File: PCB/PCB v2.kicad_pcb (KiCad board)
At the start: 4 copper layers, 56 x 45 mm, 99 parts, among them J2 USB_C_Receptacle_PowerOnly_6P, J3 6871XX182122_687110182122, J5 Conn_01x03_Pin, J7 Conn_01x07_Pin, U1 TPD2E2U06DCK, U11 OPA4350EA_250, U12 OPA4350EA_250, U13 OPA4350EA_250, U4 LM27762, U5 AD7606, U6 OPA4350EA_250

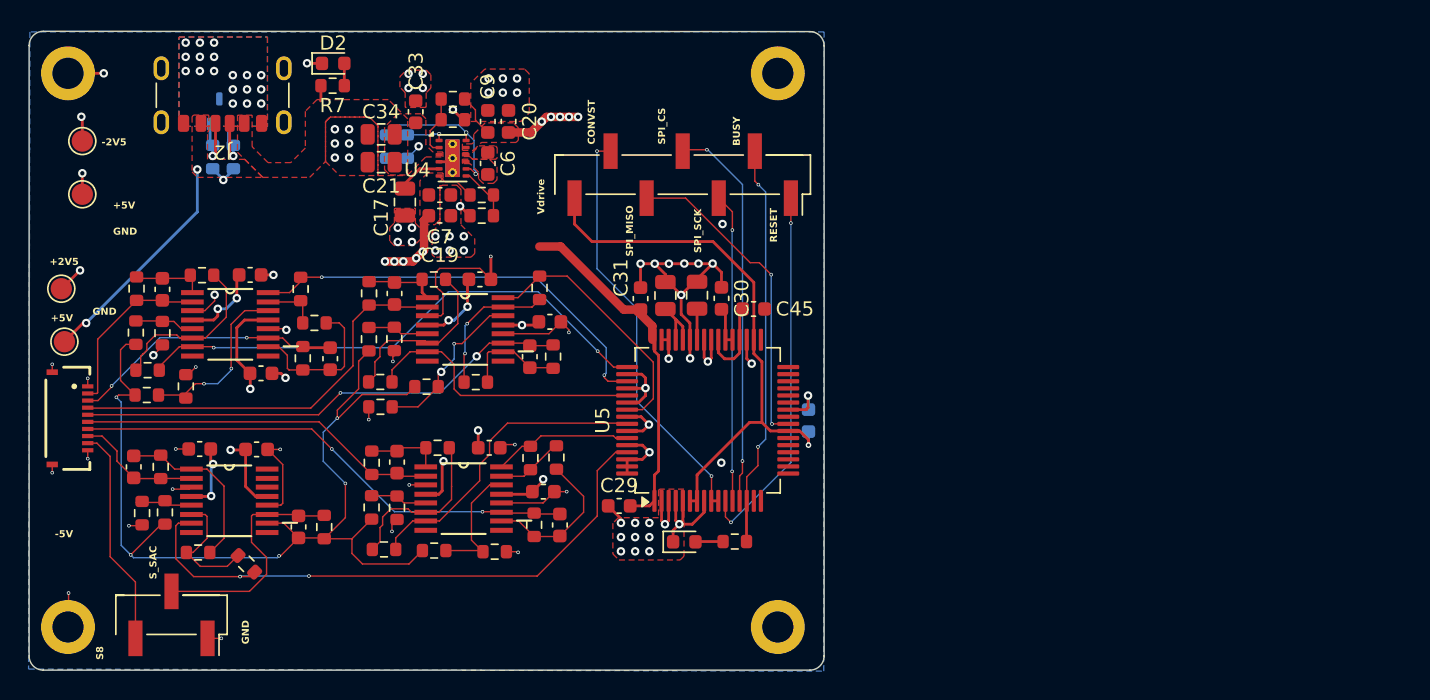
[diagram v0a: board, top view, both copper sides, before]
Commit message: Lay out the analog front-end: op-amp groups, sensor inputs, GND guard
Board work since d215e9c. The schematic changes were brought in with
Update PCB from Schematic; op-amp placement and some routing were done
by hand in pcbnew; the rest was scripted through the KiCad IPC API and
checked with offline DRC.

Op-amp groups (TIA and difference amps):
- U6: its Rf/Cf pairs sit right at each section's -IN/OUT pads, with the
  +2V5/-2V5 decoupling caps (C22/C11) on the bottom under the chip.
- U13: U6's placement, fan-out tracks and vias copied exactly
  (40 segments, 4 vias). Section mapping is A->A (S1->S7), B->B
  (S2->S_sac), C->C (S3->S5), D->D (S4->S6); C27/C28 are on the bottom.
- U11: the left half (CH1/CH2) was placed and routed by hand. The right
  half (CH3/CH4) is its mirror about the IC centre line, with pins
  1<->16, 2<->15, 3<->14, 5<->12, 6<->11 and 7<->10 (8 passives, C24,
  23 segments, 6 vias).
- U12: U11 copied at an offset of (-21.35, +3.00). CH1-3 became CH5-7
  (14 passives on the bottom, 42 segments, 13 vias). CH4's copper was
  not copied, because U12 section D is the spare. The spare is tied as a
  follower: pin 15 to pin 16 (SPARE_D), and pin 14 to a new GND via.
- U6 and U13 were then moved next to J3, U6 above and U13 below.

Sensor inputs J3 -> TIA nodes (S1-S7):
- All on F.Cu at 0.1 mm, with no vias and no crossings. Each trace
  enters its node at the Rf/Cf pad, never at the op-amp pin. Corners
  were rounded by hand.
- S1/S2 run up the left of U6 and over the top to C10/C12. S3-S6 use
  the corridor between U6 and U13, into C14/C13/C16/C15. S7 runs down
  the left of U13 and under it to C18.
- The routes were checked in an offline DRC before being applied: no
  new clearance, edge or hole violations.

GND guard around the inputs:
- New F.Cu zone GND_AFE_GUARD (priority 1, clearance 0.2, solid pad
  connection, islands removed). It covers x 125.9-136.6 and
  y 86.6-118.9, with a notch that takes in J3's GND pins.
- 31 GND stitching vias (0.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
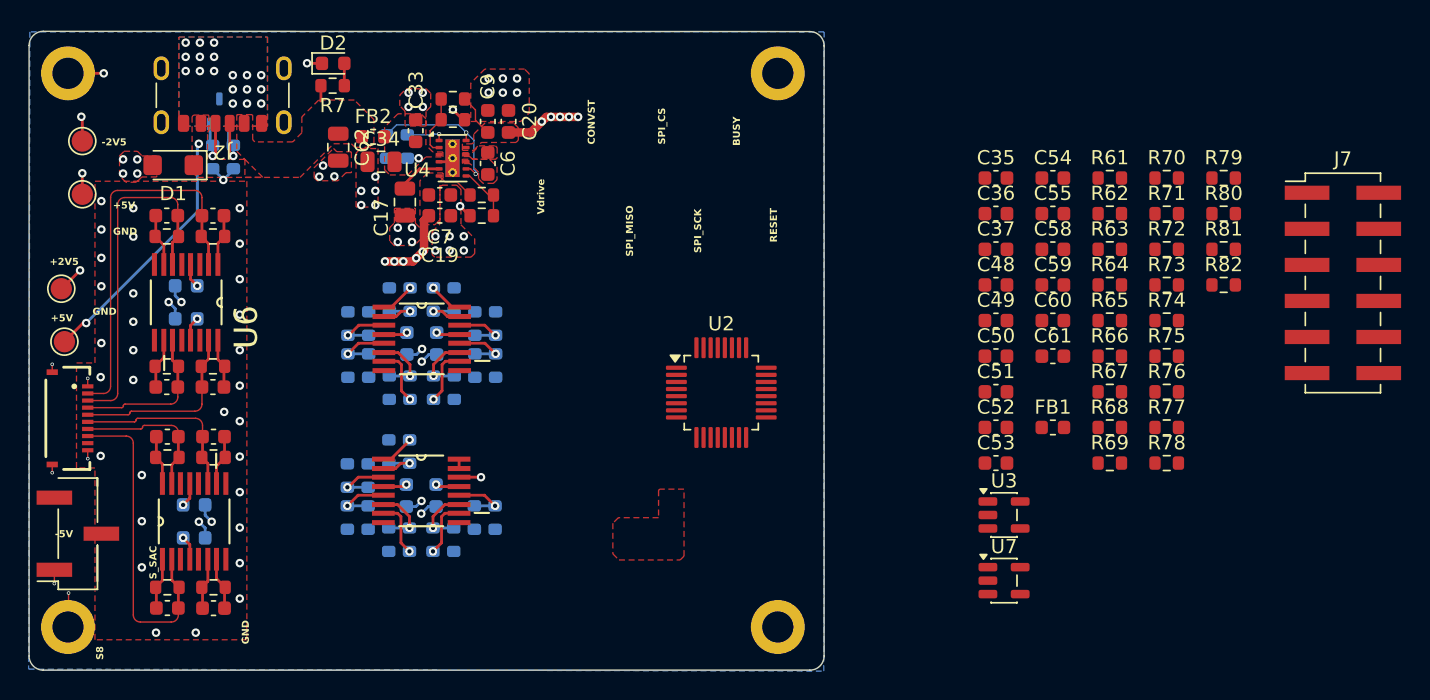
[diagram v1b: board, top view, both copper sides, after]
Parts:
- removed C21, C46, C47: 10u, Capacitor_SMD:C_0805_2012Metric
- removed C29, C30, C31, C32: 100n, Capacitor_SMD:C_0603_1608Metric
- removed C45: 1u, Capacitor_SMD:C_0603_1608Metric
- removed D3: LED, LED_SMD:LED_0603_1608Metric
- removed R8: 4.7k, Resistor_SMD:R_0603_1608Metric
- removed U5: AD7606, Package_QFP:LQFP-64_10x10mm_P0.5mm
- added C35: 220n, Capacitor_SMD:C_0603_1608Metric, F.Cu at (189.4, 86.4)
- added C36: 1u, Capacitor_SMD:C_0603_1608Metric, F.Cu at (189.4, 88.9)
- added C37: 1u, Capacitor_SMD:C_0603_1608Metric, F.Cu at (189.4, 91.4)
- added C48: 10n C0G, Capacitor_SMD:C_0603_1608Metric, F.Cu at (189.4, 93.9)
- added C49: 10n C0G, Capacitor_SMD:C_0603_1608Metric, F.Cu at (189.4, 96.4)
- added C50: 10n C0G, Capacitor_SMD:C_0603_1608Metric, F.Cu at (189.4, 98.9)
- added C51: 10n C0G, Capacitor_SMD:C_0603_1608Metric, F.Cu at (189.4, 101.4)
- added C52: 10n C0G, Capacitor_SMD:C_0603_1608Metric, F.Cu at (189.4, 103.9)
- added C53: 10n C0G, Capacitor_SMD:C_0603_1608Metric, F.Cu at (189.4, 106.5)
- added C54: 10n C0G, Capacitor_SMD:C_0603_1608Metric, F.Cu at (193.4, 86.4)
- added C55: 10n C0G, Capacitor_SMD:C_0603_1608Metric, F.Cu at (193.4, 88.9)
- added C58: 100n, Capacitor_SMD:C_0603_1608Metric, F.Cu at (193.4, 91.4)
- added C59: 100n, Capacitor_SMD:C_0603_1608Metric, F.Cu at (193.4, 93.9)
- added C60: 1u, Capacitor_SMD:C_0603_1608Metric, F.Cu at (193.4, 96.4)
- added C61: 1u, Capacitor_SMD:C_0603_1608Metric, F.Cu at (193.4, 98.9)
- added C62: 22u 16V, Capacitor_SMD:C_0805_2012Metric, F.Cu at (143.0, 84.2)
- added D1: SMF5.0A, Diode_SMD:D_SMF, F.Cu at (131.4, 85.5)
- added FB1: BLM18PG221SN1, Inductor_SMD:L_0603_1608Metric, F.Cu at (193.4, 103.9)
- added FB2: BLM18KG102SN1, Inductor_SMD:L_0603_1608Metric, F.Cu at (145.5, 83.5)
- added R61: 1.1k, Resistor_SMD:R_0603_1608Metric, F.Cu at (197.4, 86.4)
- added R62: 1k, Resistor_SMD:R_0603_1608Metric, F.Cu at (197.4, 88.9)
- added R63: 1.1k, Resistor_SMD:R_0603_1608Metric, F.Cu at (197.4, 91.4)
- added R64: 1k, Resistor_SMD:R_0603_1608Metric, F.Cu at (197.4, 93.9)
- added R65: 1.1k, Resistor_SMD:R_0603_1608Metric, F.Cu at (197.4, 96.4)
- added R66: 1k, Resistor_SMD:R_0603_1608Metric, F.Cu at (197.4, 98.9)
- added R67: 1.1k, Resistor_SMD:R_0603_1608Metric, F.Cu at (197.4, 101.4)
- added R68: 1k, Resistor_SMD:R_0603_1608Metric, F.Cu at (197.4, 103.9)
- added R69: 1.1k, Resistor_SMD:R_0603_1608Metric, F.Cu at (197.4, 106.5)
- added R70: 1k, Resistor_SMD:R_0603_1608Metric, F.Cu at (201.4, 86.4)
- added R71: 1.1k, Resistor_SMD:R_0603_1608Metric, F.Cu at (201.4, 88.9)
- added R72: 1k, Resistor_SMD:R_0603_1608Metric, F.Cu at (201.4, 91.4)
- added R73: 1.1k, Resistor_SMD:R_0603_1608Metric, F.Cu at (201.4, 93.9)
- added R74: 1k, Resistor_SMD:R_0603_1608Metric, F.Cu at (201.4, 96.4)
- added R75: 1.1k, Resistor_SMD:R_0603_1608Metric, F.Cu at (201.4, 98.9)
- added R76: 1k, Resistor_SMD:R_0603_1608Metric, F.Cu at (201.4, 101.4)
- added R77: 10k, Resistor_SMD:R_0603_1608Metric, F.Cu at (201.4, 103.9)
- added R78: 10k, Resistor_SMD:R_0603_1608Metric, F.Cu at (201.4, 106.5)
- added R79: 100k, Resistor_SMD:R_0603_1608Metric, F.Cu at (205.4, 86.4)
- added R80: 33R, Resistor_SMD:R_0603_1608Metric, F.Cu at (205.4, 88.9)
- added R81: 33R, Resistor_SMD:R_0603_1608Metric, F.Cu at (205.4, 91.4)
- added R82: 33R, Resistor_SMD:R_0603_1608Metric, F.Cu at (205.4, 93.9)
- added U2: ADS131M08xPBS, Package_QFP:TQFP-32_5x5mm_P0.5mm, F.Cu at (170.0, 101.5)
- added U3: 74LVC1G17, Package_TO_SOT_SMD:SOT-23-5, F.Cu at (189.9, 110.1)
- added U7: LP5907MFX-3.3, Package_TO_SOT_SMD:SOT-23-5, F.Cu at (189.9, 114.7)
- C11, C22, C23, C24, C25, C26, C27, C28, R24, R26, R29, R31, R34, R36, R38, R39, R44, R46, R48, R49, R56, R59: moved to B.Cu
- J7: value Conn_01x07_Pin -> Conn_02x06_Odd_Even; footprint Connector_PinHeader_2.54mm:PinHeader_1x07_P2.54mm_Vertical_SMD_Pin1Right -> Connector_PinHeader_2.54mm:PinHeader_2x06_P2.54mm_Vertical_SMD
- R23, R25, R28, R30, R33, R35, R40, R41, R43, R45, R50, R51, R55, R60: value 5k -> 4.99k; moved to B.Cu
- moved J7 47.1 mm to (213.8, 93.8), turned to 0 degrees
- moved C15 28.3 mm to (131.0, 104.6), turned to 180 degrees
- moved R42 26.3 mm to (131.0, 106.1), turned to 180 degrees
- moved R56 24.9 mm to (154.1, 110.3), turned to -90 degrees
- moved R32 24.0 mm to (134.2, 99.6), turned to 0 degrees
- moved C13 22.4 mm to (134.2, 101.1), turned to 0 degrees
- moved R55 21.8 mm to (152.6, 110.3), turned to 90 degrees
- moved R24 19.2 mm to (148.1, 94.9), turned to 90 degrees
- moved R60 18.0 mm to (151.2, 111.8), turned to 90 degrees
- moved C14 17.3 mm to (131.0, 101.1), turned to 180 degrees
- moved R25 16.4 mm to (145.2, 96.6)
- moved R30 15.8 mm to (145.2, 99.6), turned to 90 degrees
- moved C12 15.3 mm to (131.0, 89.0), turned to 180 degrees
- moved R37 15.1 mm to (131.0, 99.6), turned to 180 degrees
- moved R23 13.3 mm to (146.6, 94.9), turned to -90 degrees
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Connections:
- C10 pad 1: /SENSORS/out_a1 -> S1
- C10 pad 2: S1 -> /SENSORS/Q1
- C12 pad 1: /SENSORS/out_b1 -> S2
- C12 pad 2: S2 -> /SENSORS/Q2
- C13 pad 1: out_b2 -> S4
- C13 pad 2: S4 -> /SENSORS/Q4
- C14 pad 1: out_a2 -> S3
- C14 pad 2: S3 -> /SENSORS/Q3
- C15 pad 1: /SENSORS/out_b3 -> S6
- C15 pad 2: S6 -> /SENSORS/Q6
- C16 pad 1: /SENSORS/out_a3 -> S5
- C16 pad 2: S5 -> /SENSORS/Q5
- C18 pad 1: /SENSORS/out_a4 -> S7
- C18 pad 2: S7 -> /SENSORS/Q7
- C33 pad 1: +5V -> /POWER SUPPLY - ADC - SACRIFIED SENSOR/+5V_CP
- C34 pad 1: +5V -> /POWER SUPPLY - ADC - SACRIFIED SENSOR/+5V_CP
- C8 pad 1: /SENSORS/V_sac -> S_sac
- C8 pad 2: S_sac -> /POWER SUPPLY - ADC - SACRIFIED SENSOR/Vsac
- J7 pad 1: /POWER SUPPLY - ADC - SACRIFIED SENSOR/RESET -> GND
- J7 pad 2: /POWER SUPPLY - ADC - SACRIFIED SENSOR/BUSY -> /POWER SUPPLY - ADC - SACRIFIED SENSOR/MCU_CLK
- J7 pad 3: /POWER SUPPLY - ADC - SACRIFIED SENSOR/SPI_SCK -> GND
- J7 pad 4: /POWER SUPPLY - ADC - SACRIFIED SENSOR/SPI_CS -> /POWER SUPPLY - ADC - SACRIFIED SENSOR/ADC_SCLK
- J7 pad 5: /POWER SUPPLY - ADC - SACRIFIED SENSOR/SPI_MISO -> /POWER SUPPLY - ADC - SACRIFIED SENSOR/ADC_MOSI
- J7 pad 6: /POWER SUPPLY - ADC - SACRIFIED SENSOR/CONVST -> GND
- J7 pad 7: /POWER SUPPLY - ADC - SACRIFIED SENSOR/Vdrive -> /POWER SUPPLY - ADC - SACRIFIED SENSOR/ADC_MISO
- R10 pad 1: /SENSORS/V_sac -> S_sac
- R10 pad 2: S_sac -> /POWER SUPPLY - ADC - SACRIFIED SENSOR/Vsac
- R11 pad 1: +5V -> /POWER SUPPLY - ADC - SACRIFIED SENSOR/+5V_CP
- R12 pad 1: +5V -> /POWER SUPPLY - ADC - SACRIFIED SENSOR/+5V_CP
- R22 pad 1: /SENSORS/out_a1 -> S1
- R22 pad 2: S1 -> /SENSORS/Q1
- R23 pad 1: /SENSORS/in-_b1 -> /SENSORS/Q1
- R23 pad 2: /SENSORS/out_a1 -> /SENSORS/D1N
- R24 pad 1: /SENSORS/in-_b1 -> /SENSORS/D1N
- R25 pad 1: Net-(U6-+IN_B) -> /POWER SUPPLY - ADC - SACRIFIED SENSOR/Vsac
- R25 pad 2: /SENSORS/V_sac -> /SENSORS/D1P
- R26 pad 1: GND -> /SENSORS/D1P
- R26 pad 2: Net-(U6-+IN_B) -> GND
- R27 pad 1: /SENSORS/out_b1 -> S2
- R27 pad 2: S2 -> /SENSORS/Q2
- R28 pad 1: /SENSORS/in-_c1 -> /SENSORS/Q2
- R28 pad 2: /SENSORS/out_b1 -> /SENSORS/D2N
- R29 pad 1: /SENSORS/in-_c1 -> /SENSORS/D2N
- R30 pad 1: Net-(U6-+IN_D) -> /POWER SUPPLY - ADC - SACRIFIED SENSOR/Vsac
- R30 pad 2: /SENSORS/V_sac -> /SENSORS/D2P
- R31 pad 1: GND -> /SENSORS/D2P
- R31 pad 2: Net-(U6-+IN_D) -> GND
- R32 pad 1: out_b2 -> S4
- R32 pad 2: S4 -> /SENSORS/Q4
- R33 pad 1: Net-(U11-+IN_D) -> /POWER SUPPLY - ADC - SACRIFIED SENSOR/Vsac
- R33 pad 2: /SENSORS/V_sac -> /SENSORS/D4P
- R34 pad 1: GND -> /SENSORS/D4P
- R34 pad 2: Net-(U11-+IN_D) -> GND
- R35 pad 1: Net-(U11-+IN_B) -> /POWER SUPPLY - ADC - SACRIFIED SENSOR/Vsac
- R35 pad 2: /SENSORS/V_sac -> /SENSORS/D3P
- R36 pad 1: GND -> /SENSORS/D3P
- R36 pad 2: Net-(U11-+IN_B) -> GND
- R37 pad 1: out_a2 -> S3
- R37 pad 2: S3 -> /SENSORS/Q3
- R38 pad 1: in-_c2 -> /SENSORS/D4N
- R39 pad 1: in-_b2 -> /SENSORS/D3N
- R40 pad 1: in-_b2 -> /SENSORS/Q3
- R40 pad 2: out_a2 -> /SENSORS/D3N
- R41 pad 1: in-_c2 -> /SENSORS/Q4
- R41 pad 2: out_b2 -> /SENSORS/D4N
- R42 pad 1: /SENSORS/out_b3 -> S6
- R42 pad 2: S6 -> /SENSORS/Q6
- R43 pad 1: Net-(U12-+IN_D) -> /POWER SUPPLY - ADC - SACRIFIED SENSOR/Vsac
- R43 pad 2: /SENSORS/V_sac -> /SENSORS/D6P
- R44 pad 1: GND -> /SENSORS/D6P
- R44 pad 2: Net-(U12-+IN_D) -> GND
- R45 pad 1: Net-(U12-+IN_B) -> /POWER SUPPLY - ADC - SACRIFIED SENSOR/Vsac
- R45 pad 2: /SENSORS/V_sac -> /SENSORS/D5P
- R46 pad 1: GND -> /SENSORS/D5P
- R46 pad 2: Net-(U12-+IN_B) -> GND
- R47 pad 1: /SENSORS/out_a3 -> S5
- R47 pad 2: S5 -> /SENSORS/Q5
- R48 pad 1: /SENSORS/in-_c3 -> /SENSORS/D6N
- R49 pad 1: /SENSORS/in-_b3 -> /SENSORS/D5N
- R50 pad 1: /SENSORS/out_a3 -> /SENSORS/Q5
- R50 pad 2: /SENSORS/in-_b3 -> /SENSORS/D5N
- R51 pad 1: /SENSORS/in-_c3 -> /SENSORS/Q6
- R51 pad 2: /SENSORS/out_b3 -> /SENSORS/D6N
- R55 pad 1: Net-(U13-+IN_B) -> /POWER SUPPLY - ADC - SACRIFIED SENSOR/Vsac
- R55 pad 2: /SENSORS/V_sac -> /SENSORS/D7P
- R56 pad 1: GND -> /SENSORS/D7P
- R56 pad 2: Net-(U13-+IN_B) -> GND
- R57 pad 1: /SENSORS/out_a4 -> S7
- R57 pad 2: S7 -> /SENSORS/Q7
- R59 pad 1: /SENSORS/in-_b4 -> /SENSORS/D7N
- R60 pad 1: /SENSORS/in-_b4 -> /SENSORS/Q7
- R60 pad 2: /SENSORS/out_a4 -> /SENSORS/D7N
- U11 pad 1: out_a2 -> Vout1
- U11 pad 10: out_b2 -> Vout3
- U11 pad 11: S4 -> /SENSORS/D3N
- U11 pad 12: GND -> /SENSORS/D3P
- U11 pad 14: Net-(U11-+IN_D) -> /SENSORS/D4P
- U11 pad 15: in-_c2 -> /SENSORS/D4N
- U11 pad 2: S3 -> /SENSORS/D1N
- U11 pad 3: GND -> /SENSORS/D1P
- U11 pad 5: Net-(U11-+IN_B) -> /SENSORS/D2P
- U11 pad 6: in-_b2 -> /SENSORS/D2N
- U11 pad 7: Vout3 -> Vout2
- U12 pad 1: /SENSORS/out_a3 -> Vout5
- U12 pad 10: /SENSORS/out_b3 -> Vout7
- U12 pad 11: S6 -> /SENSORS/D7N
- U12 pad 12: GND -> /SENSORS/D7P
- U12 pad 14: Net-(U12-+IN_D) -> GND
- U12 pad 15: /SENSORS/in-_c3 -> /SENSORS/SPARE_D
- U12 pad 16: Vout6 -> /SENSORS/SPARE_D
- U12 pad 2: S5 -> /SENSORS/D5N
- U12 pad 3: GND -> /SENSORS/D5P
- U12 pad 5: Net-(U12-+IN_B) -> /SENSORS/D6P
- U12 pad 6: /SENSORS/in-_b3 -> /SENSORS/D6N
- U12 pad 7: Vout5 -> Vout6
- U13 pad 1: /SENSORS/out_a4 -> /SENSORS/Q7
- U13 pad 10: /SENSORS/V_sac -> /SENSORS/Q5
- U13 pad 11: S_sac -> S5
- U13 pad 14: unconnected-(U13-+IN_D-Pad14) -> GND
- U13 pad 15: unconnected-(U13--IN_D-Pad15) -> S6
- U13 pad 16: unconnected-(U13-OUT_D-Pad16) -> /SENSORS/Q6
- U13 pad 5: Net-(U13-+IN_B) -> GND
- U13 pad 6: /SENSORS/in-_b4 -> S_sac
- U13 pad 7: Vout7 -> /POWER SUPPLY - ADC - SACRIFIED SENSOR/Vsac
- U4 pad 3: +5V -> /POWER SUPPLY - ADC - SACRIFIED SENSOR/+5V_CP
- U6 pad 1: /SENSORS/out_a1 -> /SENSORS/Q1
- U6 pad 10: /SENSORS/out_b1 -> /SENSORS/Q3
- U6 pad 11: S2 -> S3
- U6 pad 14: Net-(U6-+IN_D) -> GND
- U6 pad 15: /SENSORS/in-_c1 -> S4
- U6 pad 16: Vout2 -> /SENSORS/Q4
- U6 pad 5: Net-(U6-+IN_B) -> GND
- U6 pad 6: /SENSORS/in-_b1 -> S2
- U6 pad 7: Vout1 -> /SENSORS/Q2
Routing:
- net GND: track 115.7 -> 27.3 mm, vias 103 -> 102
- net /SENSORS/V_sac: track 70.5 -> 0.00 mm, vias 5 -> 0
- net /POWER SUPPLY - ADC - SACRIFIED SENSOR/Vdrive: track 39.8 -> 0.00 mm, vias 1 -> 0
- net Vout7: track 42.5 -> 4.03 mm, vias 2 -> 1
- net Vout1: track 37.4 -> 2.43 mm, vias 2 -> 1
- net /POWER SUPPLY - ADC - SACRIFIED SENSOR/CONVST: track 29.4 -> 0.00 mm, vias 2 -> 0
- net +5V: track 47.5 -> 19.1 mm, vias 3 -> 2
- net /POWER SUPPLY - ADC - SACRIFIED SENSOR/BUSY: track 28.4 -> 0.00 mm, vias 2 -> 0
- net /POWER SUPPLY - ADC - SACRIFIED SENSOR/SPI_CS: track 27.5 -> 0.00 mm, vias 2 -> 0
- net Vout2: track 30.4 -> 4.03 mm, vias 2 -> 1
- net /POWER SUPPLY - ADC - SACRIFIED SENSOR/RESET: track 26.3 -> 0.00 mm, vias 2 -> 0
- net S6: track 35.5 -> 10.6 mm, vias 2 -> 0
- net /POWER SUPPLY - ADC - SACRIFIED SENSOR/SPI_MISO: track 22.7 -> 0.00 mm, vias 2 -> 0
- net /POWER SUPPLY - ADC - SACRIFIED SENSOR/SPI_SCK: track 21.7 -> 0.00 mm, vias 2 -> 0
- net S4: track 34.7 -> 13.2 mm, vias 2 -> 0
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- added copper zone on F.Cu, net /POWER SUPPLY - ADC - SACRIFIED SENSOR/+5V_CP

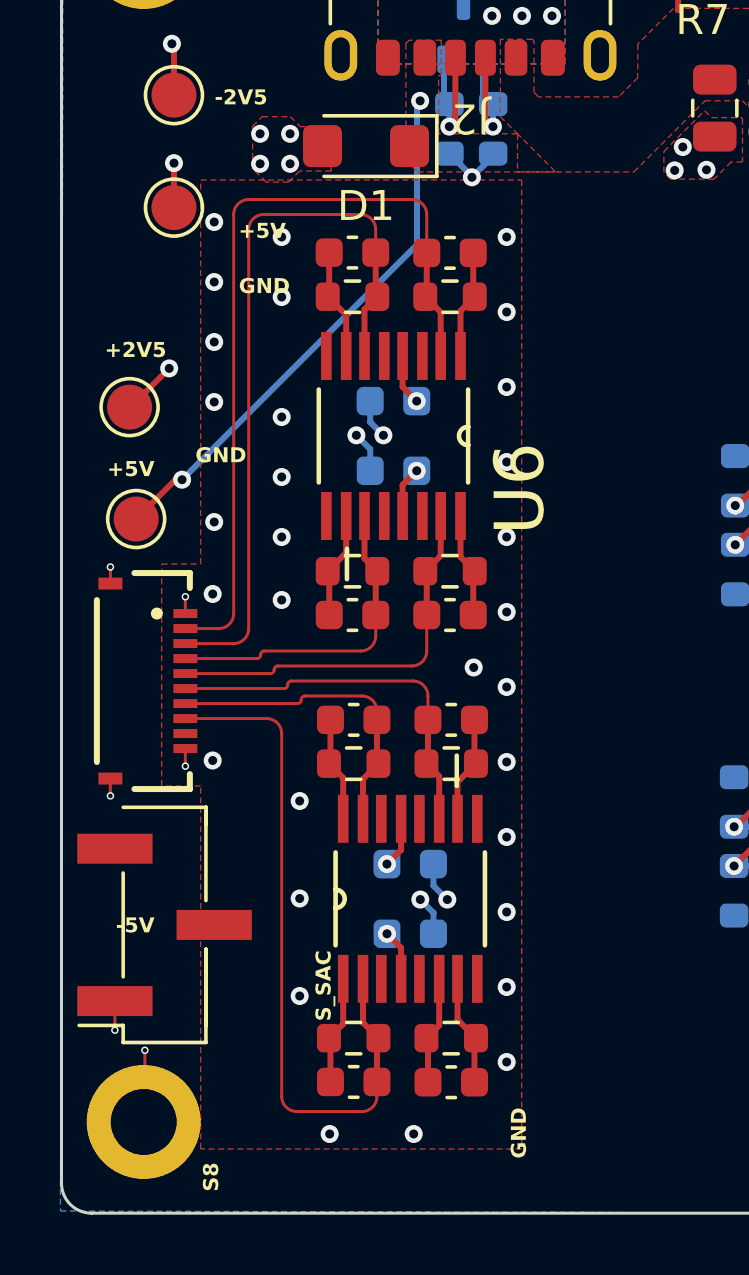
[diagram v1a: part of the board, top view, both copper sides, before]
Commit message: Place 1.27 mm J5 next to U13 and route S8 / S_sac inside the GND guard
J5 footprint update (from the schematic change) and placement:
- J5 is now the 1.27 mm SMD header, at (125.85, 111.98), rotated 90
  degrees. It sits left of U13, between J3 and mounting hole H3, inside
  the board outline.
- Pin 1 (GND) keeps its own GND via, moved to (124.59, 112.63) with a
  short stub to the pad; this replaces the old via at (123.04, 114.94).

S8, J3 pin 9 -> J5 pin 3 (F.Cu, 0.1 mm):
- Leaves J3 pin 9 horizontally at y 105.05, between S7 (J3 pin 8) and
  J3 pin 10 (GND), with 0.4 / 0.3 mm gaps.
- Turns down with a 0.5 mm radius arc and runs straight at x 127.12 into
  J5 pin 3.
- The whole trace stays inside GND_AFE_GUARD, left of S7's vertical run
  at x 128.6, with guard copper filling the gap between them.

S_sac, J5 pin 2 -> C8 pin 1 / R10 pin 1 / U13 pin 6 (F.Cu, 0.1 mm):
- S7 runs around the whole left and bottom side of U13 (its loop closes
  at C18). J5 pin 2, on the far side of that loop, cannot reach U13's
  S_sac pin on F.Cu without crossing it.
- Rather than hop through B.Cu (the -2V5 pour) with two vias on a sensor
  input, S_sac goes around the bottom of the loop:
  - down from J5 pin 2;
  - a 45 degree jog to x 126.45, which keeps about 0.5 mm from H3's
    3.8 mm GND pad;
  - down to y 118.4, below S7's bottom run at 117.65 (0.65 mm gap);
  - right along y 118.4;
  - up into C8 pin 1 from below, joining the existing C8 -> R10 -> U13
    pin 6 trace.
- The 90 degree turns are 0.5 mm arcs, like the other sensor traces.
- There are no vias and no layer change.

GND guard adjustments, so S_sac is guarded underneath:
- GND_AFE_GUARD bottom edge moved from y 118.9 to y 120.4 (the board
  edge is at y 121.04).
- The two stitching vias at (130.2, 118.4) and (133.0, 118.4) were on the
  new path. They are replaced by a row of four GND vias (0.6 / 0.3) at
  y 119.6: x 127.5 / 130.2 / 133.0 / 135.8.
- Zones refilled.

Verification:
- The patch was trial-applied to a snap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
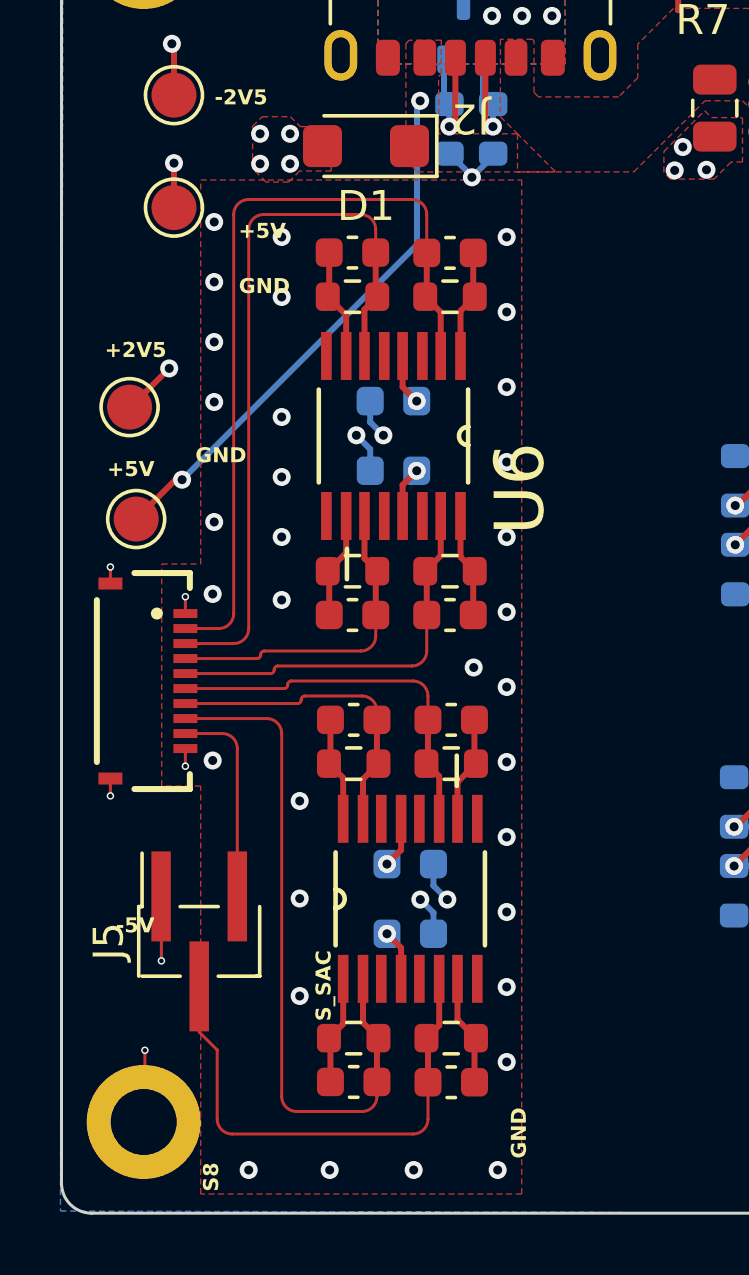
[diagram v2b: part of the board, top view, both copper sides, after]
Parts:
- J5: footprint Connector_PinHeader_2.54mm:PinHeader_1x03_P2.54mm_Vertical_SMD_Pin1Right -> Connector_PinHeader_1.27mm:PinHeader_1x03_P1.27mm_Vertical_SMD_Pin1Right
- moved J5 1.28 mm to (125.8, 112.0), turned to 90 degrees
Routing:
- net S_sac: track 3.64 -> 17.1 mm
- net S8: track 0.00 -> 6.92 mm
- net GND: vias 102 -> 104
